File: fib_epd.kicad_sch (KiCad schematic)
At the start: 58 parts, among them U1 TPS651851RSLT, U1101 ESP32-S3-WROOM-1U, U601 TLV75733PDBV

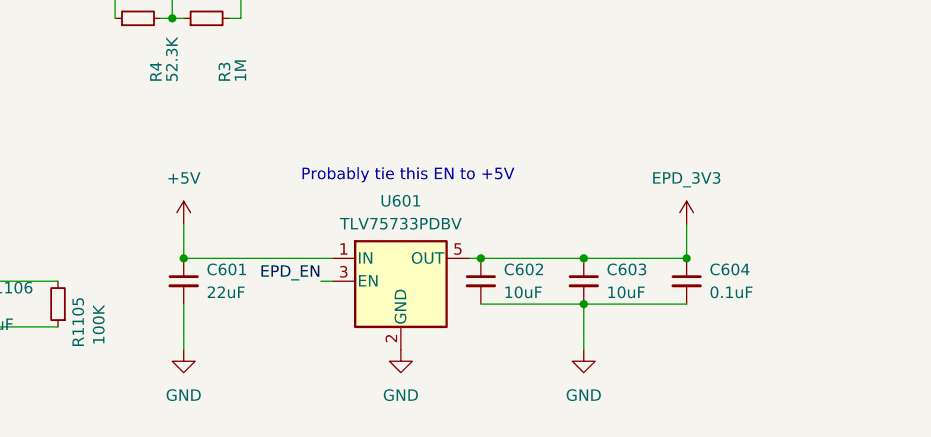
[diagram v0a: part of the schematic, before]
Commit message: started routing the SODIMM, updated connector footprint, started arranging component into sub-areas
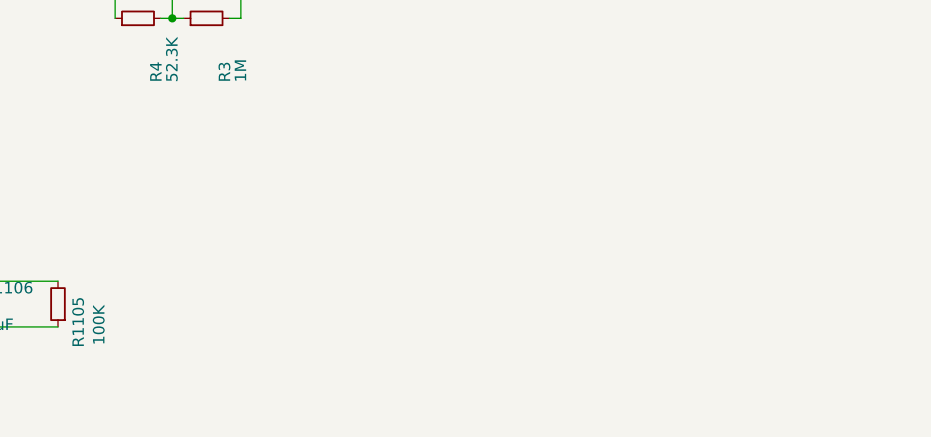
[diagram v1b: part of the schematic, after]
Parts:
- removed C601: 22uF, Capacitor_SMD:C_0805_2012Metric, symbol Device:C_Small
- removed C602, C603: 10uF, Capacitor_SMD:C_0603_1608Metric, symbol Device:C_Small
- removed C604: 0.1uF, Capacitor_SMD:C_0603_1608Metric, symbol Device:C_Small
- removed U601: TLV75733PDBV, Package_TO_SOT_SMD:SOT-23-5, symbol Regulator_Linear:TLV75733PDBV
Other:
- note removed: "Probably tie this EN to +5V"

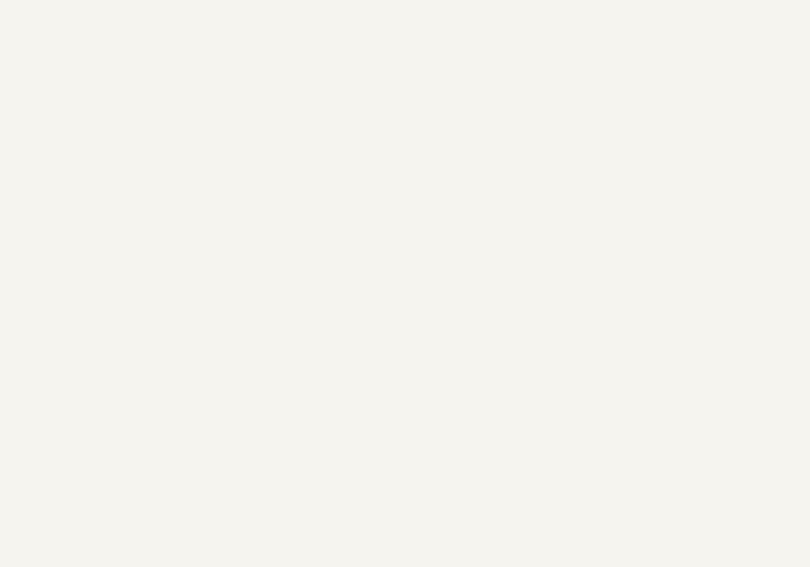
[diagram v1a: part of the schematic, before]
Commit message: did a ton of routing and modeling for SOM, USB, DP & Charging/Power, things starting to take shape
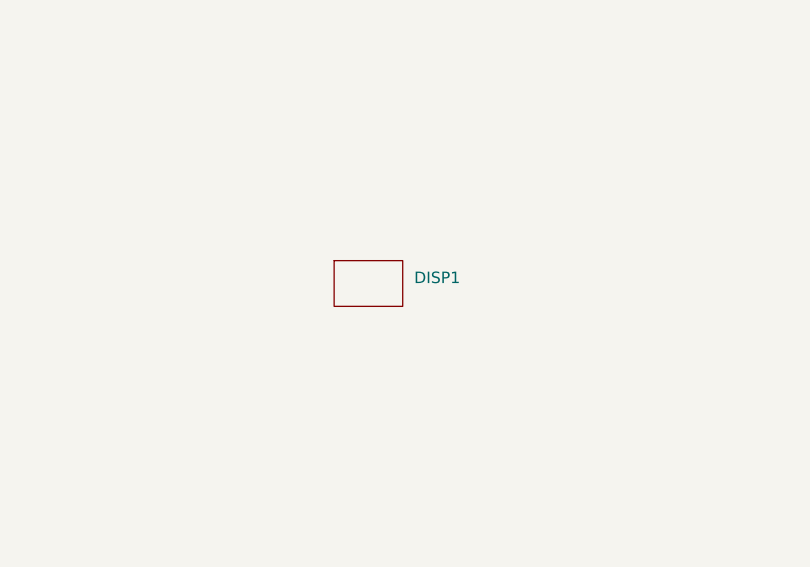
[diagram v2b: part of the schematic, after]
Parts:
- added DISP1: ~, Fibel2:7.8 EInk, symbol Fibel2:7.8_EInk
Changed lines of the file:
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@@
+	)
+	(symbol
+		(lib_id "Fibel2:7.8_EInk")
+		(at 193.04 132.08 0)
+		(unit 1)
+		(exclude_from_sim no)
+		(in_bom yes)
+		(on_board yes)
+		(dnp no)
+		(fields_autoplaced yes)
+		(property "Reference" "DISP1"
+			(at 198.12 131.4449 0)
+			(effects
+				(font
+					(size 1.27 1.27)
+				)
+				(justify left)
+			)
+		)
+		(property "Value" "~"
+			(at 198.12 133.35 0)
+			(effects
+				(font
+					(size 1.27 1.27)
+				)
+				(justify left)
+			)
+		)
+		(property "Footprint" "Fibel2:7.8 EInk"
+			(at 193.04 132.08 0)
+			(effects
+				(font
+					(size 1.27 1.27)
+				)
+				(hide yes)
+			)
+		)
+		(property "Datasheet" ""
+			(at 193.04 132.08 0)
+			(effects
+				(font
+					(size 1.27 1.27)
+				)
+				(hide yes)
+			)
+		)
+		(property "Description" ""
+			(at 193.04 132.08 0)
+			(effects
+				(font
+					(size 1.27 1.27)
+				)
+				(hide yes)
+			)
+		)
+		(instances
+			(project ""
+				(path "/862c21e2-7ec9-4f80-a33c-aad02ea9423e/5a179277-42b3-47ed-bc0e-bf53dbccdf92"
+					(reference "DISP1")
+					(unit 1)
+				)
+			)
+		)
 	)
 	(symbol

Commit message: implemented most of USB and Power Supplies
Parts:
- C1, C10, C11, C1107, C12, C13, C14, C15, C16, C17, C18, C19, C2, C20, C22, C7, C8, C9: footprint Capacitor_SMD:C_0805_2012Metric -> Capacitor_SMD:C_0402_1005Metric
- C23: footprint Capacitor_SMD:C_0805_2012Metric -> Capacitor_SMD:C_0603_1608Metric
- R1101, R1102, R1103, R1104, R1105, R1106, R1107, R4, R5, R6, R7: footprint Resistor_SMD:R_0603_1608Metric -> Resistor_SMD:R_0402_1005Metric
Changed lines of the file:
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@@
 			)
 		)
-		(property "Footprint" "Capacitor_SMD:C_0805_2012Metric"
+		(property "Footprint" "Capacitor_SMD:C_0402_1005Metric"
 			(at 50.8 97.79 0)
 			(effects
@@
 			)
 		)
-		(property "Footprint" "Resistor_SMD:R_0603_1608Metric"
+		(property "Footprint" "Resistor_SMD:R_0402_1005Metric"
 			(at 52.07 156.21 0)
 			(effects
@@
 			)
 		)
-		(property "Footprint" "Capacitor_SMD:C_0805_2012Metric"
+		(property "Footprint" "Capacitor_SMD:C_0402_1005Metric"
 			(at 69.85 119.38 0)
 			(effects
@@
 			)
 		)
-		(property "Footprint" "Resistor_SMD:R_0603_1608Metric"
+		(property "Footprint" "Resistor_SMD:R_0402_1005Metric"
 			(at 19.05 180.34 0)
 			(effects
@@
 			)
 		)
-		(property "Footprint" "Resistor_SMD:R_0603_1608Metric"
+		(property "Footprint" "Resistor_SMD:R_0402_1005Metric"
 			(at 90.17 180.34 0)
 			(effects
@@
 			)
 		)
-		(property "Footprint" "Capacitor_SMD:C_0805_2012Metric"
+		(property "Footprint" "Capacitor_SMD:C_0402_1005Metric"
 			(at 20.32 97.79 0)
 			(effects
@@
 			)
 		)
-		(property "Footprint" "Capacitor_SMD:C_0805_2012Metric"
+		(property "Footprint" "Capacitor_SMD:C_0402_1005Metric"
 			(at 60.96 97.79 0)
 			(effects
@@
 			)
 		)
-		(property "Footprint" "Resistor_SMD:R_0603_1608Metric"
+		(property "Footprint" "Resistor_SMD:R_0402_1005Metric"
 			(at 194.31 46.99 0)
 			(effects
@@
 			)
 		)
-		(property "Footprint" "Capacitor_SMD:C_0805_2012Metric"
+		(property "Footprint" "Capacitor_SMD:C_0402_1005Metric"
 			(at 157.48 30.48 0)
 			(effects
@@
 			)
 		)
-		(property "Footprint" "Resistor_SMD:R_0603_1608Metric"
+		(property "Footprint" "Resistor_SMD:R_0402_1005Metric"
 			(at 52.07 180.34 0)
 			(effects
@@
 			)
 		)
-		(property "Footprint" "Capacitor_SMD:C_0805_2012Metric"
+		(property "Footprint" "Capacitor_SMD:C_0402_1005Metric"
 			(at 53.34 34.29 0)
 			(effects
@@
 			)
 		)
-		(property "Footprint" "Capacitor_SMD:C_0805_2012Metric"
+		(property "Footprint" "Capacitor_SMD:C_0402_1005Metric"
 			(at 135.89 39.37 0)
 			(effects
@@
 			)
 		)
-		(property "Footprint" "Capacitor_SMD:C_0805_2012Metric"
+		(property "Footprint" "Capacitor_SMD:C_0402_1005Metric"
 			(at 130.81 33.02 0)
 			(effects
@@
 			)
 		)
-		(property "Footprint" "Capacitor_SMD:C_0805_2012Metric"
+		(property "Footprint" "Capacitor_SMD:C_0402_1005Metric"
 			(at 34.29 66.04 0)
 			(effects
@@
 			)
 		)
-		(property "Footprint" "Resistor_SMD:R_0603_1608Metric"
+		(property "Footprint" "Resistor_SMD:R_0402_1005Metric"
 			(at 194.31 34.29 0)
 			(effects
@@
 			)
 		)
-		(property "Footprint" "Resistor_SMD:R_0603_1608Metric"
+		(property "Footprint" "Resistor_SMD:R_0402_1005Metric"
 			(at 166.37 40.64 0)
 			(effects
@@
 			)
 		)
-		(property "Footprint" "Capacitor_SMD:C_0805_2012Metric"
+		(property "Footprint" "Capacitor_SMD:C_0402_1005Metric"
 			(at 106.68 139.7 0)
 			(effects
@@
 			)
 		)
-		(property "Footprint" "Resistor_SMD:R_0603_1608Metric"
+		(property "Footprint" "Resistor_SMD:R_0402_1005Metric"
 			(at 166.37 30.48 0)
 			(effects
@@
 			)
 		)
-		(property "Footprint" "Capacitor_SMD:C_0805_2012Metric"
+		(property "Footprint" "Capacitor_SMD:C_0402_1005Metric"
 			(at 105.41 111.76 0)
 			(effects
@@
 			)
 		)
-		(property "Footprint" "Capacitor_SMD:C_0805_2012Metric"
+		(property "Footprint" "Capacitor_SMD:C_0402_1005Metric"
 			(at 43.18 49.53 0)
 			(effects
@@
 			)
 		)
-		(property "Footprint" "Capacitor_SMD:C_0805_2012Metric"
+		(property "Footprint" "Capacitor_SMD:C_0402_1005Metric"
 			(at 50.8 49.53 0)
 			(effects
@@
 			)
 		)
-		(property "Footprint" "Resistor_SMD:R_0603_1608Metric"
+		(property "Footprint" "Resistor_SMD:R_0402_1005Metric"
 			(at 19.05 156.21 0)
 			(effects
@@
 			)
 		)
-		(property "Footprint" "Resistor_SMD:R_0603_1608Metric"
+		(property "Footprint" "Resistor_SMD:R_0402_1005Metric"
 			(at 99.06 148.59 0)
 			(effects
@@
 			)
 		)
-		(property "Footprint" "Capacitor_SMD:C_0805_2012Metric"
+		(property "Footprint" "Capacitor_SMD:C_0402_1005Metric"
 			(at 35.56 49.53 0)
 			(effects
@@
 			)
 		)
-		(property "Footprint" "Capacitor_SMD:C_0805_2012Metric"
+		(property "Footprint" "Capacitor_SMD:C_0603_1608Metric"
 			(at 26.67 72.39 0)
 			(effects
@@
 			)
 		)
-		(property "Footprint" "Capacitor_SMD:C_0805_2012Metric"
+		(property "Footprint" "Capacitor_SMD:C_0402_1005Metric"
 			(at 40.64 97.79 0)
 			(effects
@@
 			)
 		)
-		(property "Footprint" "Capacitor_SMD:C_0805_2012Metric"
+		(property "Footprint" "Capacitor_SMD:C_0402_1005Metric"
 			(at 201.93 36.83 0)
 			(effects
@@
 			)
 		)
-		(property "Footprint" "Resistor_SMD:R_0603_1608Metric"
+		(property "Footprint" "Resistor_SMD:R_0402_1005Metric"
 			(at 73.66 154.94 0)
 			(effects
@@
 			)
 		)
-		(property "Footprint" "Capacitor_SMD:C_0805_2012Metric"
+		(property "Footprint" "Capacitor_SMD:C_0402_1005Metric"
 			(at 30.48 97.79 0)
 			(effects
@@
 			)
 		)
-		(property "Footprint" "Capacitor_SMD:C_0805_2012Metric"
+		(property "Footprint" "Capacitor_SMD:C_0402_1005Metric"
 			(at 96.52 135.89 0)
 			(effects

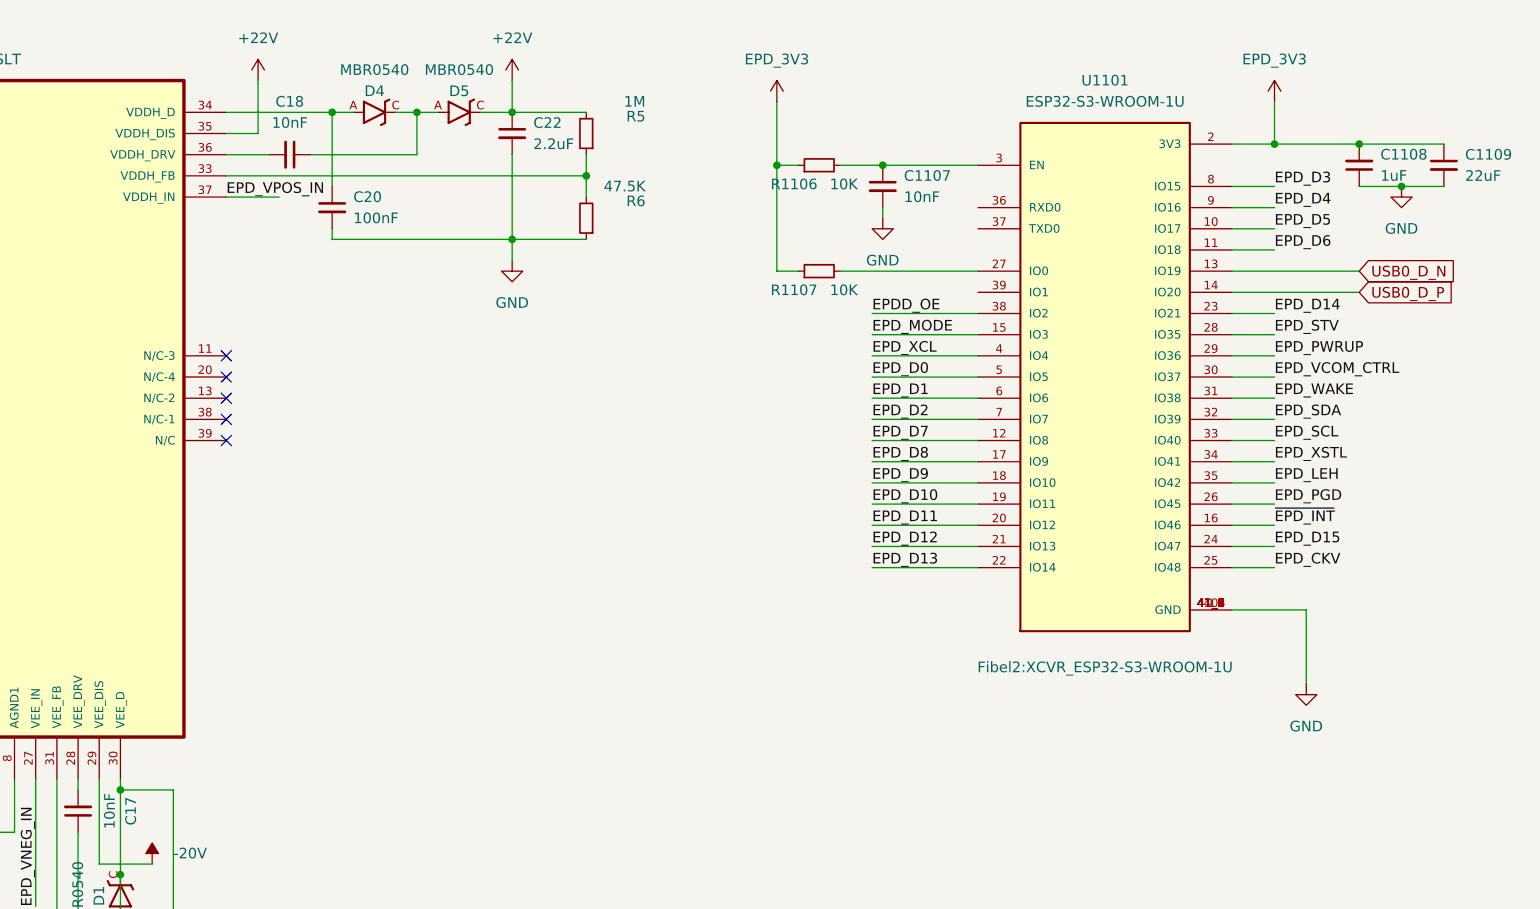
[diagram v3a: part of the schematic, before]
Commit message: did a big portion of pcie, optimized placement of components and subsections. power, usb and charging is largely done. still need to do length matching though. will need to take a second look at schemativs after routing is done
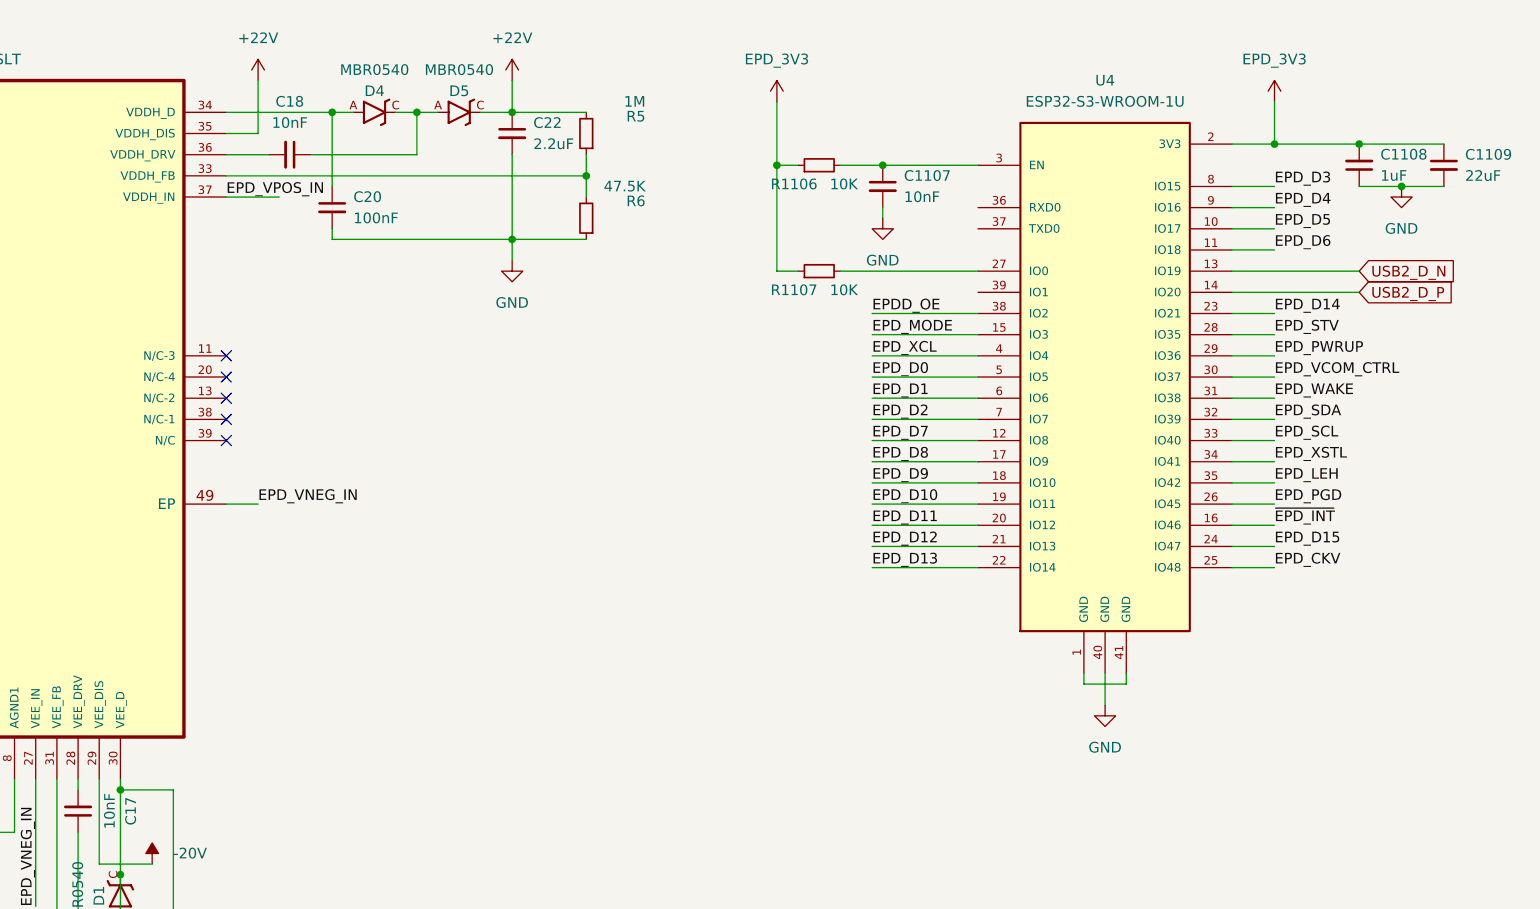
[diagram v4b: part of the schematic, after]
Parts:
- removed U1101: ESP32-S3-WROOM-1U, Fibel2:XCVR_ESP32-S3-WROOM-1U, symbol Fibel2:ESP32-S3-WROOM-1U
- added U4: ESP32-S3-WROOM-1U, Fibel2:XCVR_ESP32-S3-WROOM-1U, symbol Fibel2:ESP32-S3-WROOM-1U
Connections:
- net EPDD_OE: now also U4.38 (IO2)
- net EPD_3V3: now also U4.2 (3V3)
- net EPD_CKV: now also U4.25 (IO48)
- net EPD_D0: now also U4.5 (IO5)
- net EPD_D1: now also U4.6 (IO6)
- net EPD_D10: now also U4.19 (IO11)
- net EPD_D11: now also U4.20 (IO12)
- net EPD_D12: now also U4.21 (IO13)
- net EPD_D13: now also U4.22 (IO14)
- net EPD_D14: now also U4.23 (IO21)
- net EPD_D15: now also U4.24 (IO47)
- net EPD_D2: now also U4.7 (IO7)
- net EPD_D3: now also U4.8 (IO15)
- net EPD_D4: now also U4.9 (IO16)
- net EPD_D5: now also U4.10 (IO17)
- net EPD_D6: now also U4.11 (IO18)
- net EPD_D7: now also U4.12 (IO8)
- net EPD_D8: now also U4.17 (IO9)
- net EPD_D9: now also U4.18 (IO10)
- net EPD_LEH: now also U4.35 (IO42)
- net EPD_MODE: now also U4.15 (IO3)
- net EPD_PGD: now also U4.26 (IO45)
- net EPD_PWRUP: now also U4.29 (IO36)
- net EPD_SCL: now also U4.33 (IO40)
- net EPD_SDA: now also U4.32 (IO39)
- net EPD_STV: now also U4.28 (IO35)
- net EPD_VCOM_CTRL: now also U4.30 (IO37)
- net EPD_VNEG_IN: now also U1.49 (EP)
- net EPD_WAKE: now also U4.31 (IO38)
- net EPD_XCL: now also U4.4 (IO4)
- net EPD_XSTL: now also U4.34 (IO41)
- net GND: now also U4.40 (GND)
- net ~{EPD_INT}: now also U4.16 (IO46)
- net at R1107.2: now also U4.27 (IO0)
- net at C1107.1, R1106.2: now also U4.3 (EN)
- new net: U4.1 (GND), U4.41 (GND)
- new net USB2_D_N: U4.13 (IO19)
- new net USB2_D_P: U4.14 (IO20)

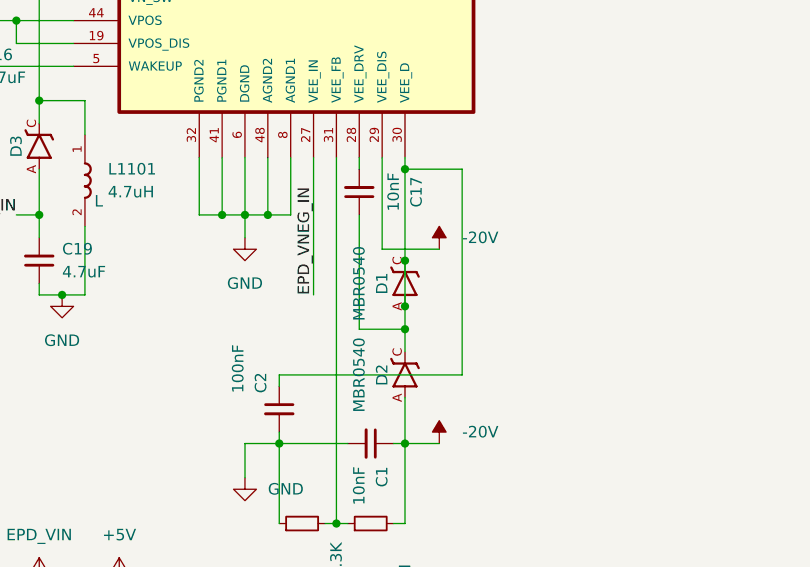
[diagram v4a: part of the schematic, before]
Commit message: further optimized placement, finished most of buck array, expanded pcie, added tons of missing footprints, diff pair spacing optimization
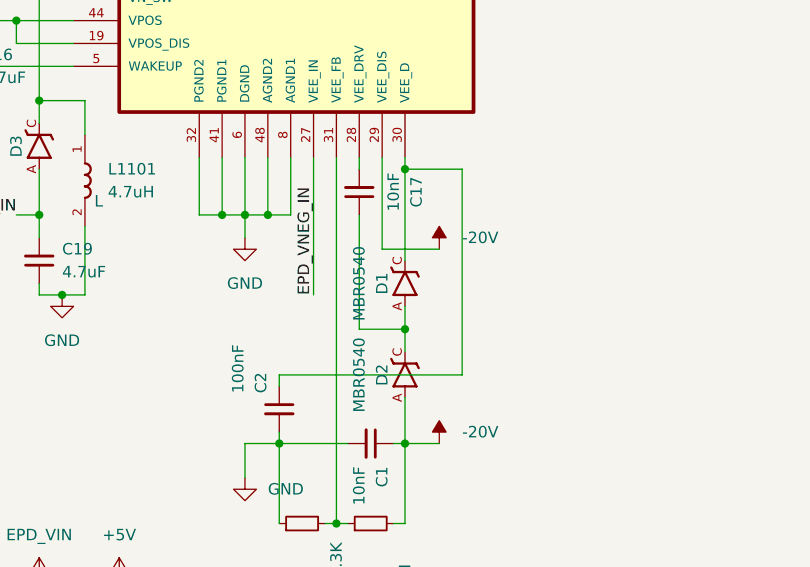
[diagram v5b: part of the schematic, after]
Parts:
- R3: footprint Resistor_SMD:R_0603_1608Metric -> Resistor_SMD:R_0402_1005Metric
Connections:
- net at C17.1, D1.A, D2.C: no longer C2.1, D1.C, U1.30 (VEE_D)
- new net: C2.1, D1.C, U1.30 (VEE_D)
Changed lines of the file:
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@@
 	)
 	(junction
-		(at 110.49 124.46)
-		(diameter 0)
-		(color 0 0 0 0)
-	)
-	(junction
 		(at 33.02 162.56)
 		(diameter 0)
@@
 	)
 	(junction
-		(at 110.49 119.38)
-		(diameter 0)
-		(color 0 0 0 0)
-	)
-	(junction
 		(at 189.23 34.29)
 		(diameter 0)
@@
 	(wire
 		(pts
-			(xy 110.49 119.38) (xy 110.49 124.46)
-		)
-		(stroke
-			(width 0)
-			(type default)
-		)
-	)
-	(wire
-		(pts
 			(xy 196.85 34.29) (xy 201.93 34.29)
 		)
@@
 			)
 		)
-		(property "Footprint" "Resistor_SMD:R_0603_1608Metric"
+		(property "Footprint" "Resistor_SMD:R_0402_1005Metric"
 			(at 106.68 148.59 0)
 			(effects
